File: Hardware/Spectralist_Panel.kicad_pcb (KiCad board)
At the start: 2 copper layers, 60.8 x 128.5 mm, 25 parts

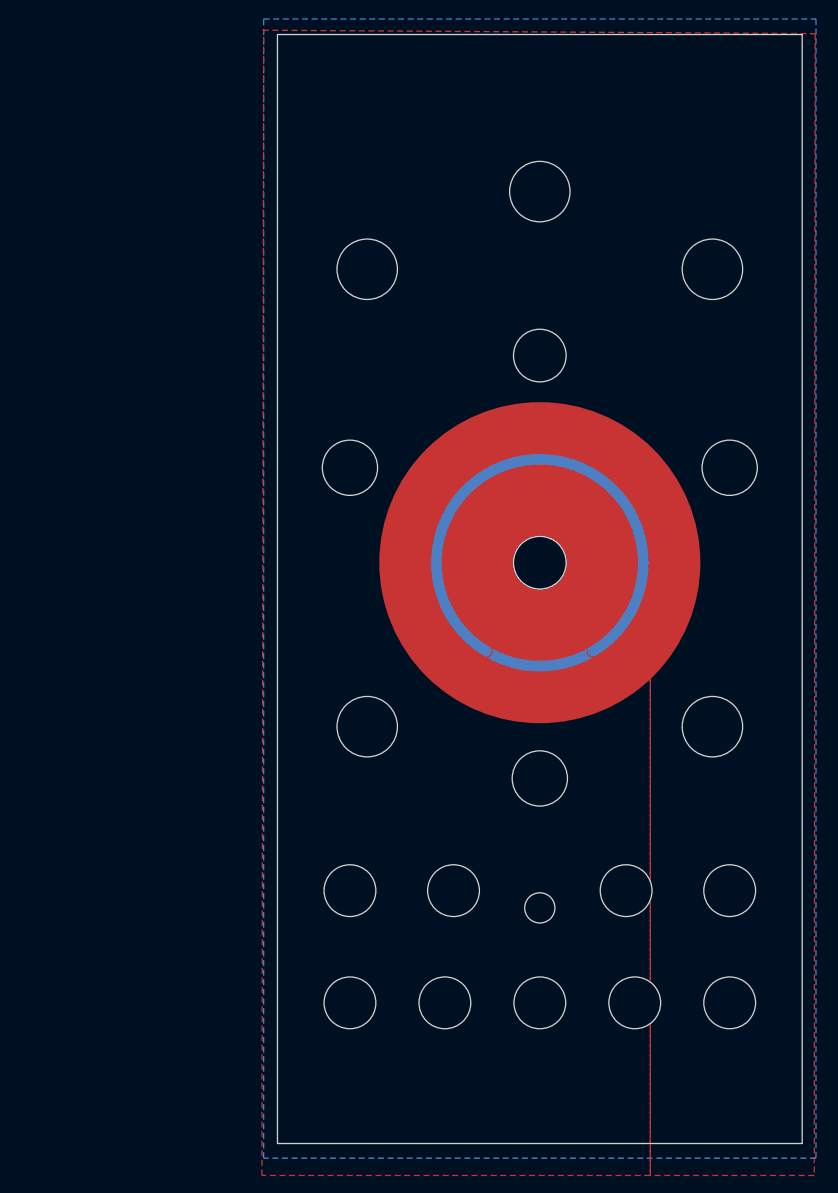
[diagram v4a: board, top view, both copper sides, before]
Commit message: Started adding JLC part numbers
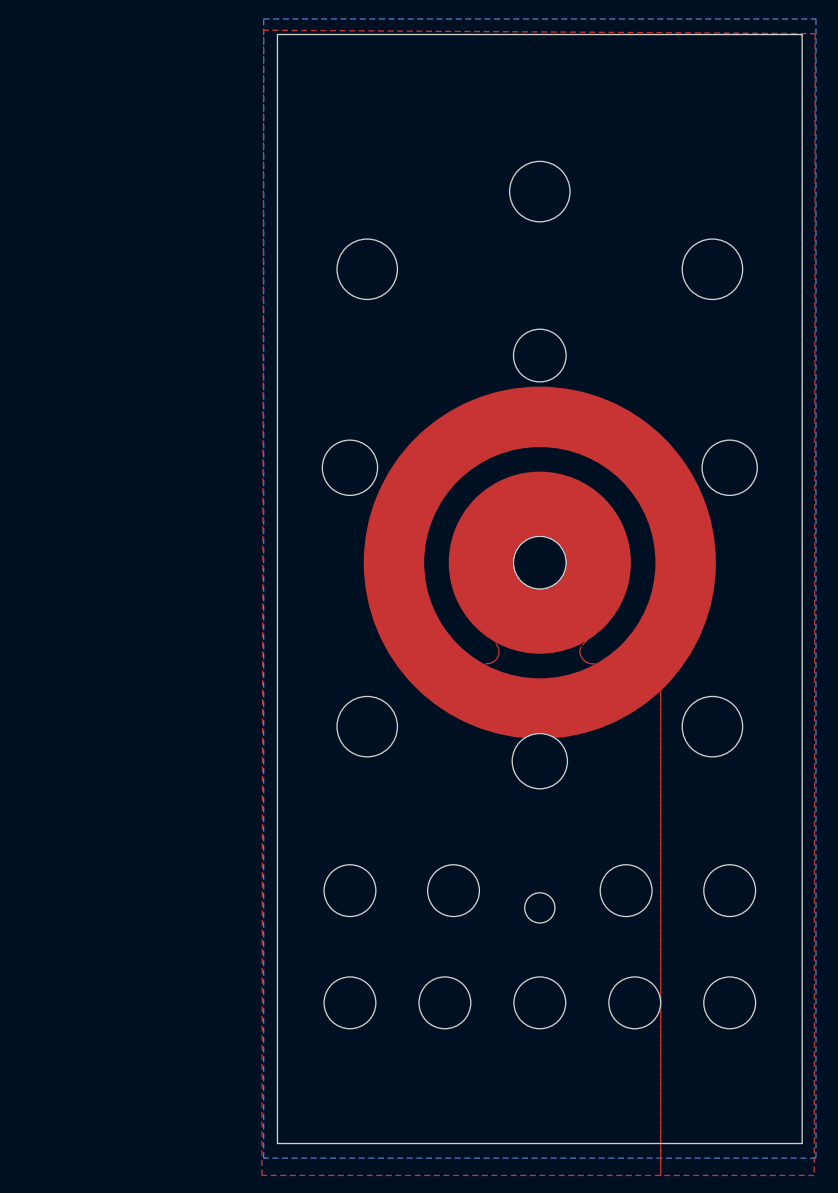
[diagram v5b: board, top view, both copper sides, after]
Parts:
- moved Ref** 2.00 mm to (130.0, 125.0)
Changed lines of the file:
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@@
 	(footprint "Custom_Footprints:Tall_Trimmer_Hole"
 		(layer "F.Cu")
-		(at 130 127)
+		(at 130 125)
 		(descr "Mounting Hole 6.5mm")
 		(tags "mounting hole 6.5mm")
@@
 	(gr_circle
 		(center 130 102)
-		(end 141.32 102)
+		(end 140.5 102)
 		(stroke
 			(width 0.1)
@@
 	(gr_circle
 		(center 130 102)
-		(end 145.6 102)
-		(stroke
-			(width 6)
+		(end 146.9 102)
+		(stroke
+			(width 7)
 			(type default)
 		)
@@
 		(net 1)
 	)
-	(gr_circle
-		(center 130 102)
-		(end 142 102)
-		(stroke
-			(width 2)
-			(type default)
-		)
-		(fill none)
-		(layer "B.Cu")
-	)
 	(gr_rect
 		(start 115.9 41.6)
@@
 		(layer "B.SilkS")
 	)
-	(gr_line
-		(start 153.7 109.6)
-		(end 155.1 108.8)
+	(gr_arc
+		(start 123.84 112.265)
+		(mid 130.033685 89.974457)
+		(end 136.1 112.3)
+		(stroke
+			(width 2.8)
+			(type default)
+		)
+		(layer "B.Mask")
+	)
+	(gr_line
+		(start 155.67 109.21)
+		(end 157.07 108.41)
 		(stroke
 			(width 1.2)
@@
 	)
 	(gr_line
-		(start 128 96)
-		(end 128 93.25)
+		(start 128 96.3)
+		(end 128 94.3)
 		(stroke
 			(width 0.5)
@@
 	)
 	(gr_line
-		(start 156.4 110.1)
-		(end 153.7 109.6)
+		(start 158.37 109.71)
+		(end 155.67 109.21)
 		(stroke
 			(width 1.2)
@@
 		(layer "F.Mask")
 	)
-	(gr_line
-		(start 103.65 107.05)
-		(end 105.15 105.55)
+	(gr_circle
+		(center 146 160.3)
+		(end 146.9 161.8)
+		(stroke
+			(width 0.1)
+			(type default)
+		)
+		(fill none)
+		(layer "F.Mask")
+	)
+	(gr_line
+		(start 103.05 109.32)
+		(end 104.55 107.82)
 		(stroke
 			(width 1.2)
@@
 	)
 	(gr_line
-		(start 127 96)
-		(end 127 93.25)
+		(start 127 96.3)
+		(end 127 94.3)
 		(stroke
 			(width 0.5)
@@
 	)
 	(gr_line
-		(start 105.15 105.55)
-		(end 106.95 106.55)
+		(start 104.55 107.82)
+		(end 106.35 108.82)
 		(stroke
 			(width 1.2)
@@
 	)
 	(gr_line
-		(start 132 96)
-		(end 132 93.25)
+		(start 132 96.3)
+		(end 132 94.3)
 		(stroke
 			(width 0.5)
 			(type default)
 		)
+		(layer "F.Mask")
+	)
+	(gr_circle
+		(center 114 160.3)
+		(end 114.9 161.8)
+		(stroke
+			(width 0.1)
+			(type default)
+		)
+		(fill none)
 		(layer "F.Mask")
 	)
@@
 	(gr_rect
 		(start 126 109.8)
-		(end 134 110.3)
+		(end 134 110.25)
 		(stroke
 			(width 0.1)
@@
 	)
 	(gr_arc
-		(start 123.841076 112.264874)
-		(mid 130.034299 90.029252)
-		(end 136.1 112.299999)
-		(stroke
-			(width 1.5)
-			(type default)
-		)
-		(layer "F.Mask")
-	)
-	(gr_line
-		(start 131 96)
-		(end 131 93.25)
+		(start 123.84 112.265)
+		(mid 130.033685 89.974457)
+		(end 136.1 112.3)
+		(locked yes)
+		(stroke
+			(width 3.8)
+			(type default)
+		)
+		(layer "F.Mask")
+	)
+	(gr_line
+		(start 131 96.3)
+		(end 131 94.3)
 		(stroke
 			(width 0.5)
@@
 	)
 	(gr_line
-		(start 130 96)
-		(end 130 93.25)
+		(start 130 96.3)
+		(end 130 94.3)
 		(stroke
 			(width 0.5)
@@
 	)
 	(gr_line
-		(start 138.8 127.5)
-		(end 139.5 125.9)
+		(start 138.75 126.82)
+		(end 139.45 125.22)
 		(stroke
 			(width 1.2)
@@
 	)
 	(gr_line
-		(start 106.95 106.55)
-		(end 103.65 107.05)
+		(start 106.35 108.82)
+		(end 103.05 109.32)
 		(stroke
 			(width 1.2)
@@
 	)
 	(gr_line
-		(start 139.5 125.9)
-		(end 140.1 128.7)
+		(start 139.45 125.22)
+		(end 140.05 128.02)
 		(stroke
 			(width 1.2)
@@
 	)
 	(gr_line
-		(start 140.1 128.7)
-		(end 138.8 127.5)
+		(start 140.05 128.02)
+		(end 138.75 126.82)
 		(stroke
 			(width 1.2)
@@
 	)
 	(gr_line
-		(start 155.1 108.8)
-		(end 156.4 110.1)
+		(start 157.07 108.41)
+		(end 158.37 109.71)
 		(stroke
 			(width 1.2)
@@
 	)
 	(gr_arc
-		(start 130.031754 127)
-		(mid 113.510184 122.044122)
-		(end 105.319064 106.864249)
+		(start 129.736482 125.679143)
+		(mid 114.47879 122.046004)
+		(end 104.78 109.72)
 		(stroke
 			(width 1)
@@
 	)
 	(gr_line
-		(start 133 96)
-		(end 133 93.25)
+		(start 133 96.3)
+		(end 133 94.3)
 		(stroke
 			(width 0.5)
@@
 	)
 	(gr_circle
-		(center 130 127)
-		(end 130 123)
+		(center 130 125)
+		(end 130 121)
 		(stroke
 			(width 0.15)
@@
 	)
 	(gr_arc
-		(start 154.923857 110.311906)
-		(mid 150 121)
-		(end 139.986297 127.181057)
+		(start 156.879508 109.846121)
+		(mid 150.940198 120.472749)
+		(end 140.23 126.26)
 		(stroke
 			(width 1)
@@
 	)
 	(gr_line
-		(start 129 96)
-		(end 129 93.25)
+		(start 129 96.3)
+		(end 129 94.3)
 		(stroke
 			(width 0.5)
@@
 	)
 	(gr_text "Filter"
-		(at 152 161.5 0)
+		(at 152.8 161.5 0)
 		(layer "F.Mask")
 		(effects
@@
 	)
 	(gr_text "Out"
-		(at 119 161.5 0)
+		(at 119.8 161.5 0)
 		(layer "F.Mask")
 		(effects
@@
 	)
 	(gr_text "Out"
-		(at 141 161.5 0)
+		(at 140.2 161.5 0)
 		(layer "F.Mask")
 		(effects
@@
 	)
 	(gr_text "Filter"
-		(at 108 161.5 0)
+		(at 107.2 161.5 0)
 		(layer "F.Mask")
 		(effects
@@
 		(polygon
 			(pts
-				(xy 97.9 40.3) (xy 161.9 40.7) (xy 161.8 173) (xy 142.8 173) (xy 142.8 89) (xy 116.8 89) (xy 116.8 114)
-				(xy 122.7 114) (xy 123.7 113) (xy 124.105385 112.906923) (xy 124.4 112.6) (xy 124.475385 112.2)
-				(xy 124.1 111) (xy 135.8 111) (xy 135.5 112) (xy 135.5 112.2) (xy 135.5 112.5) (xy 135.7 112.8)
-				(xy 136 112.9) (xy 136.2 112.9) (xy 137 113.1) (xy 137.4 113.8) (xy 142.8 114) (xy 142.8 173) (xy 97.8 173)
-				(xy 98 40.3)
+				(xy 97.9 40.3) (xy 161.9 40.7) (xy 161.8 173) (xy 144 173) (xy 144 88) (xy 115.8 88) (xy 115.75 113.85)
+				(xy 122.6 113.85) (xy 124.35 113.65) (xy 124.95 113.25) (xy 125.25 112.7) (xy 125.25 111.95) (xy 124.85 111.2)
+				(xy 135.4 111.05) (xy 134.8 111.7) (xy 134.65 112.1) (xy 134.65 112.55) (xy 134.9 113.1) (xy 135.3 113.5)
+				(xy 135.8 113.7) (xy 136.6 113.75) (xy 137.4 114) (xy 144 114) (xy 144 173) (xy 97.8 173) (xy 98 40.3)
 			)
 		)
@@
 			)
 		)
+	)
+	(zone
+		(net 0)
+		(net_name "")
+		(layer "B.Cu")
+		(hatch edge 0.5)
+		(connect_pads
+			(clearance 0)
+		)
+		(min_thickness 0.25)
+		(filled_areas_thickness no)
+		(keepout
+			(tracks not_allowed)
+			(vias not_allowed)
+			(pads not_allowed)
+			(copperpour not_allowed)
+			(footprints allowed)
+		)
+		(fill
+			(thermal_gap 0.5)
+			(thermal_bridge_width 0.5)
+		)
+		(polygon
+			(pts
+				(xy 116 88) (xy 144 88) (xy 144 114) (xy 116 114)
+			)
+		)

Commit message: v1.0 PCBs sent to production
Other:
- board text added: "Mountjoy Modular 2025 Sinosaur Panel v1.0"
- board text removed: "Mountjoy Modular 2024 Sinosaur Panel v2.0"
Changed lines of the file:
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@@
 	)
 	(gr_line
-		(start 130.031383 137.4)
-		(end 130.031383 143.8)
+		(start 130 136)
+		(end 130 142)
 		(stroke
 			(width 0.6)
@@
 	)
 	(gr_line
+		(start 160.1 41)
+		(end 160.1 168.8)
+		(stroke
+			(width 0.6)
+			(type default)
+		)
+		(layer "F.Mask")
+	)
+	(gr_line
+		(start 99.9 41.4)
+		(end 99.9 169.2)
+		(stroke
+			(width 0.6)
+			(type default)
+		)
+		(layer "F.Mask")
+	)
+	(gr_line
 		(start 131 96.3)
 		(end 131 94.3)
@@
 		)
 	)
-	(gr_text "Mountjoy Modular 2024\nSinosaur Panel v2.0"
+	(gr_text "Mountjoy Modular 2025\nSinosaur Panel v1.0"
 		(at 129.8 44.5 0)
 		(layer "B.SilkS")
@@
 		(polygon
 			(pts
-				(xy 128.897317 134.860871) (xy 129.440323 134.496166) (xy 130.031382 134.394937) (xy 130.664606 134.4969)
-				(xy 131.162192 134.864128) (xy 131.530824 135.36208) (xy 131.631383 135.994937) (xy 131.531906 136.587115)
-				(xy 131.163582 137.127136) (xy 130.66491 137.452581) (xy 130.031383 137.594937) (xy 129.440316 137.452596)
-				(xy 128.9 137.12632) (xy 128.574409 136.586667) (xy 128.431383 135.994937) (xy 128.570888 135.360621)
+				(xy 128.865935 134.860871) (xy 129.408941 134.496166) (xy 130 134.394937) (xy 130.633224 134.4969)
+				(xy 131.13081 134.864128) (xy 131.499442 135.36208) (xy 131.600001 135.994937) (xy 131.500524 136.587115)
+				(xy 131.1322 137.127136) (xy 130.633528 137.452581) (xy 130.000001 137.594937) (xy 129.408934 137.452596)
+				(xy 128.868618 137.12632) (xy 128.543027 136.586667) (xy 128.400001 135.994937) (xy 128.539506 135.360621)
 			)
 		)
@@
 		(polygon
 			(pts
-				(xy 128.570888 135.360621) (xy 128.897317 134.860871) (xy 129.440323 134.496166) (xy 130.031383 134.394937)
-				(xy 130.664606 134.4969) (xy 131.162192 134.864128) (xy 131.530824 135.36208) (xy 131.631383 135.994937)
-				(xy 131.531906 136.587115) (xy 131.163582 137.127136) (xy 130.66491 137.452581) (xy 130.031383 137.594937)
-				(xy 129.440316 137.452596) (xy 128.9 137.12632) (xy 128.574409 136.586667) (xy 128.431383 135.994937)
-			)
-		)
+				(xy 128.539506 135.360621) (xy 128.865935 134.860871) (xy 129.408941 134.496166) (xy 130.000001 134.394937)
+				(xy 130.633224 134.4969) (xy 131.13081 134.864128) (xy 131.499442 135.36208) (xy 131.600001 135.994937)
+				(xy 131.500524 136.587115) (xy 131.1322 137.127136) (xy 130.633528 137.452581) (xy 130.000001 137.594937)
+				(xy 129.408934 137.452596) (xy 128.868618 137.12632) (xy 128.543027 136.586667) (xy 128.400001 135.994937)
+			)
+		)

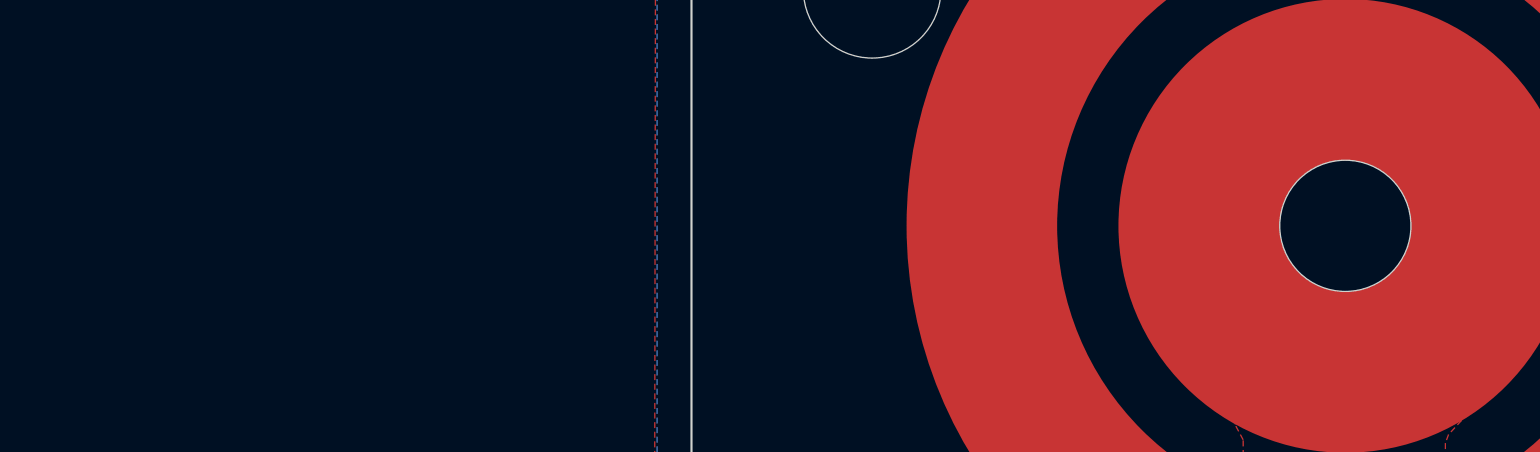
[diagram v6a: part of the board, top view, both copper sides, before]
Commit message: Updated panel with correct sub-miniature switch hole size
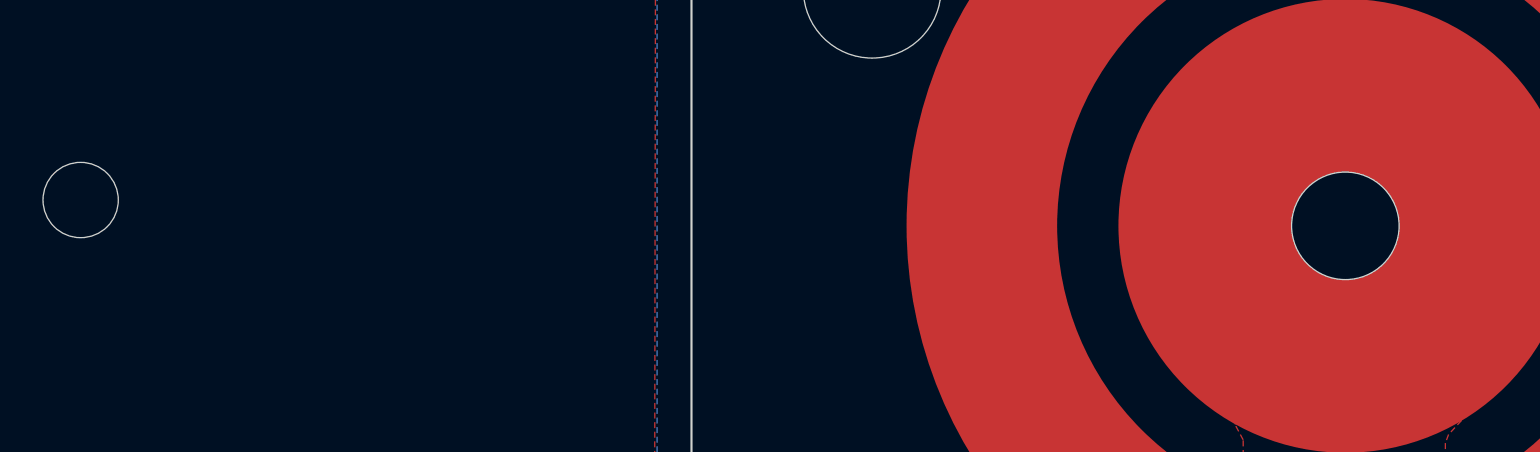
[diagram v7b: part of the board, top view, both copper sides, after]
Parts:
- added Ref**: Subminiature_Switch, Custom_Footprints:Sub_Miniature_Switch_MountingHole_3.5mm, F.Cu at (71.2, 100.8)
- Ref**: footprint Custom_Footprints:MountingHole_6.1mm -> Custom_Footprints:Sub_Miniature_Switch_MountingHole_5mm
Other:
- board text added: "Mountjoy Modular 2025 Sinosaur Panel v2.0"
- board text removed: "Mountjoy Modular 2025 Sinosaur Panel v1.0"
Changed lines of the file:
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@@
 		)
 	)
-	(footprint "Custom_Footprints:MountingHole_6.1mm"
+	(footprint "Custom_Footprints:Sub_Miniature_Switch_MountingHole_5mm"
 		(layer "F.Cu")
 		(at 130 102)
@@
 		(tags "mounting hole 6mm no annular")
 		(property "Reference" "Ref**"
-			(at 0.5 -5.6 0)
+			(at 0 -5.4 0)
 			(layer "F.SilkS")
 			(hide yes)
@@
 		)
 		(property "Value" "Thonkikonn_6.1mm"
-			(at 0.2 5.8 0)
+			(at 0 5.1 0)
 			(layer "F.Fab")
+			(hide yes)
 			(effects
 				(font
@@
 			)
 		)
-		(property "Footprint" ""
+		(property "Footprint" "Custom_Footprints:Sub_Miniature_Switch_MountingHole_5mm"
 			(at 0 0 0)
-			(unlocked yes)
 			(layer "F.Fab")
 			(hide yes)
@@
 		(property "Datasheet" ""
 			(at 0 0 0)
-			(unlocked yes)
 			(layer "F.Fab")
 			(hide yes)
@@
 		(property "Description" ""
 			(at 0 0 0)
-			(unlocked yes)
 			(layer "F.Fab")
 			(hide yes)
@@
 		(fp_circle
 			(center 0 0)
-			(end 2.93 0)
+			(end 2.5 0)
 			(stroke
 				(width 0.15)
@@
 		(fp_circle
 			(center 0 0)
-			(end 4.3 0)
+			(end 4 0)
 			(stroke
 				(width 0.05)
@@
 		(pad "" np_thru_hole circle
 			(at 0 0)
-			(size 6.1 6.1)
-			(drill 6.1)
-			(layers "F&B.Cu" "*.Mask" "F.SilkS")
+			(size 5 5)
+			(drill 5)
+			(layers "*.Cu" "*.Mask")
 		)
 		(model "${CUSTOM_3D}/Eledis 1A11-NF1STSE SPDT Toggle Switch.stp"
 			(offset
-				(xyz 0 4.7 -13.1)
+				(xyz 0 3.8 -12)
 			)
 			(scale
-				(xyz 1 1 1)
+				(xyz 0.8 0.8 0.8)
 			)
 			(rotate
@@
 			)
 			(scale
-				(xyz 1 1 1)
+				(xyz 0.87 0.87 0.87)
 			)
 			(rotate
@@
 		)
 	)
+	(footprint "Custom_Footprints:Sub_Miniature_Switch_MountingHole_3.5mm"
+		(layer "F.Cu")
+		(at 71.2 100.8)
+		(descr "Mounting Hole 6mm, no annular")
+		(tags "mounting hole 6mm no annular")
+		(property "Reference" "Ref**"
+			(at 0 -5.4 0)
+			(layer "F.SilkS")
+			(hide yes)
+			(effects
+				(font
+					(size 1 1)
+					(thickness 0.15)
+				)
+			)
+		)
+		(property "Value" "Subminiature_Switch"
+			(at 0 5.1 0)
+			(layer "F.Fab")
+			(hide yes)
+			(effects
+				(font
+					(size 1 1)
+					(thickness 0.15)
+				)
+			)
+		)
+		(property "Footprint" "Custom_Footprints:Sub_Miniature_Switch_MountingHole_3.5mm"
+			(at 0 0 0)
+			(layer "F.Fab")
+			(hide yes)
+			(effects
+				(font
+					(size 1.27 1.27)
+					(thickness 0.15)
+				)
+			)
+		)
+		(property "Datasheet" ""
+			(at 0 0 0)
+			(layer "F.Fab")
+			(hide yes)
+			(effects
+				(font
+					(size 1.27 1.27)
+					(thickness 0.15)
+				)
+			)
+		)
+		(property "Description" ""
+			(at 0 0 0)
+			(layer "F.Fab")
+			(hide yes)
+			(effects
+				(font
+					(size 1.27 1.27)
+					(thickness 0.15)
+				)
+			)
+		)
+		(attr through_hole)
+		(fp_circle
+			(center 0 0)
+			(end 1.5 0)
+			(stroke
+				(width 0.15)
+				(type solid)
+			)
+			(fill none)
+			(layer "Cmts.User")
+		)
+		(fp_circle
+			(center 0 0)
+			(end 1.6 0)
+			(stroke
+				(width 0.05)
+				(type solid)
+			)
+			(fill none)
+			(layer "F.CrtYd")
+		)
+		(pad "" np_thru_hole circle
+			(at 0 0)
+			(size 3.5 3.5)
+			(drill 3.5)
+			(layers "*.Cu" "*.Mask")
+		)
+	)
 	(footprint "Custom_Footprints:Thonkiconn_Socket_MountingHole_6mm"
 		(layer "F.Cu")
@@
 		)
 	)
-	(gr_text "Mountjoy Modular 2025\nSinosaur Panel v1.0"
+	(gr_text "Mountjoy Modular 2025\nSinosaur Panel v2.0"
 		(at 129.8 44.5 0)
 		(layer "B.SilkS")
